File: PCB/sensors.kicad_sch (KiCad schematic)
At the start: 29 parts, among them U10 INIR2-ME5, U11 110-507, U12 110-303, U5 ADS1015IDGS, U6 BME688, U7 MCP6042, U8 MCP6042, U9 MCP6042

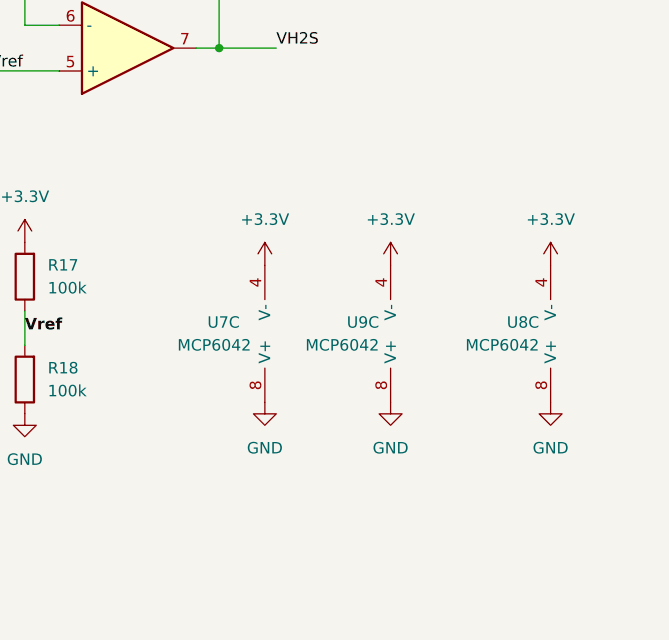
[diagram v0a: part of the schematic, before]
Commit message: Fixed op amp short bug
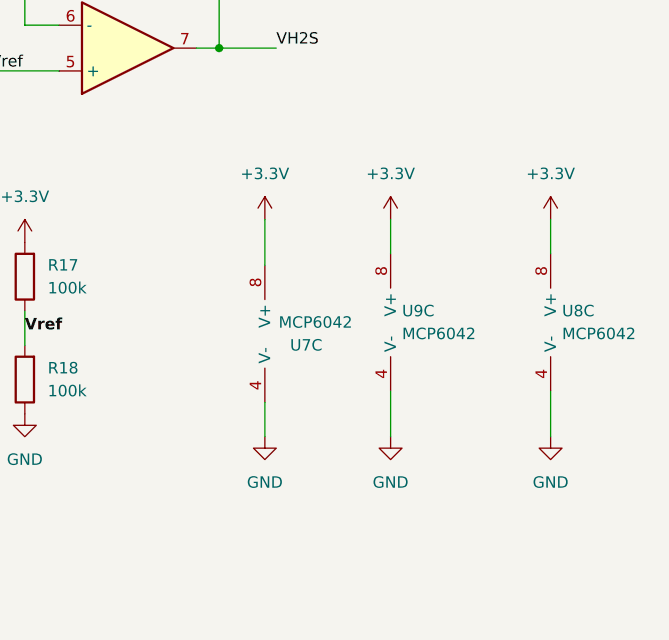
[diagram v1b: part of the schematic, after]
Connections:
- net +3.3V: now also U7.8 (V+), U8.8 (V+), U9.8 (V+); no longer U7.4 (V-), U8.4 (V-), U9.4 (V-)
- net GND: now also U7.4 (V-), U8.4 (V-), U9.4 (V-); no longer U7.8 (V+), U8.8 (V+), U9.8 (V+)
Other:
- moved on the sheet: U7C, U8C, U9C

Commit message: Started work on collecting data from sensors
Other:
- note added: "Addr: 0x49"
- note removed: "Addr: 0x48"
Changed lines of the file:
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@@
 		)
 	)
-	(text "Addr: 0x48"
+	(text "Addr: 0x49"
 		(exclude_from_sim no)
 		(at 80.01 148.844 0)

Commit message: Updated fuse and started work on talking with CH4 sensor
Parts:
- F1: footprint Fuse:Fuse_0603_1608Metric -> Fuse:Fuse_1206_3216Metric; Manufacturer Part Number F0603G0R12FNTR -> 0466.125NRHF
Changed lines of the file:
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@@
 			)
 		)
-		(property "Footprint" "Fuse:Fuse_0603_1608Metric"
+		(property "Footprint" "Fuse:Fuse_1206_3216Metric"
 			(at 168.91 147.828 90)
 			(effects
@@
 			)
 		)
-		(property "Manufacturer Part Number" "F0603G0R12FNTR"
+		(property "Manufacturer Part Number" "0466.125NRHF"
 			(at 168.91 146.05 90)
 			(effects
